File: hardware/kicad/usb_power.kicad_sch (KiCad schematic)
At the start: 9 parts, among them J801 USB-C, U801 USBLC6-2SC6, U802 LM66100DCKR

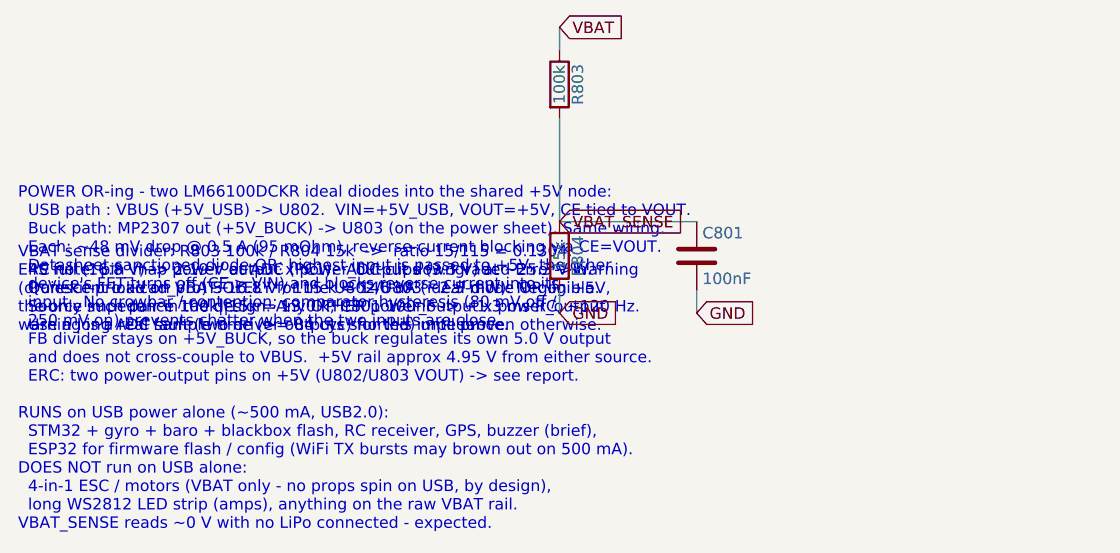
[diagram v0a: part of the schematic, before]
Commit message: Design review fixes: EN divider, +5V OR sizing, +5V bulk
- R106 43k -> 39k: MP2307 EN lockout 2.5V typ gives ~8.9 V turn-on and
  keeps EN < 6 V abs-max to 20 V input (was 6.0 V, zero margin)
- U803 LM66100 -> LM74700 + Q803 AO3400A: 1.5 A ceiling was below the
  ~1.9 A worst-case +5V budget; now FET-limited ~5 A at ~53 mV
- C113 22uF on the +5V OR node (was ~2 uF of LDO input caps only)
- ERC power_output x power_output reverted to Error; +5V now has a
  single power-output pin

Co-Authored-By: Claude Sonnet 5 <noreply@anthropic.com>
Claude-Session: https://claude.ai/code/session_0171uwNh8K8uwZuWio9f35u1
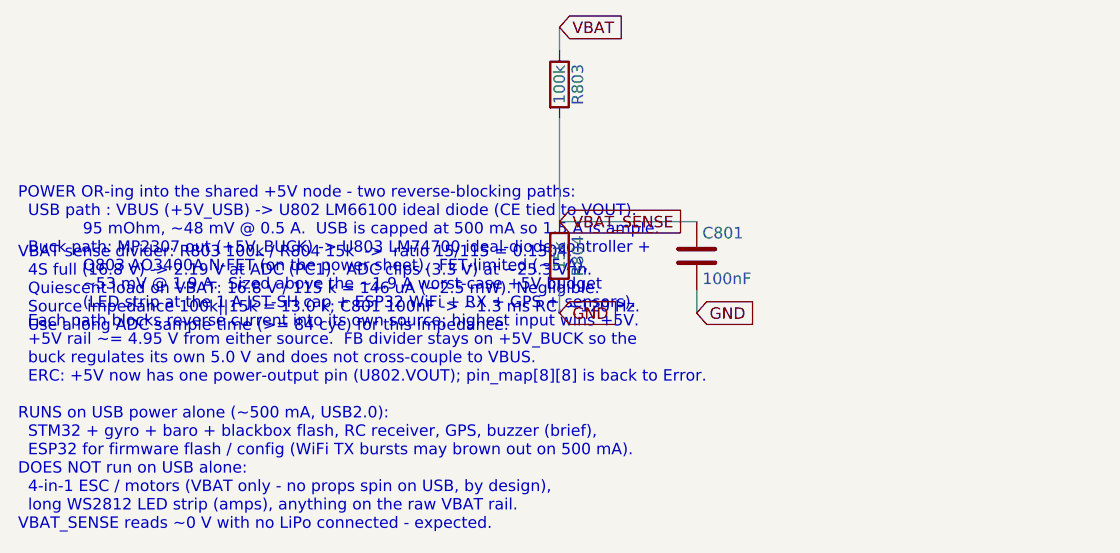
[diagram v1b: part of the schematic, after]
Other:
- note added: "POWER OR-ing into the shared +5V node - two reverse-blocking paths: USB path : VBUS (+5V_USB) -> U802 LM66100 ideal diode (CE tied to VOUT). 95 mOhm, ~48 mV @ 0.5 A. USB is capped at 500 mA so 1.5 A is ample. Buck path: MP2307 out (+5V_BUCK) -> U803 LM74700 ideal-diode controller + Q803 AO3400A N-FET (on the power sheet). FET-limited (~5 A), ~53 mV @ 1.9 A. Sized above the ~1.9 A worst-case +5V b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"
- note removed: "ERC note: pin_map power_output x power_output downgraded Error->Warning (dronekit-pro.kicad_pro) SOLELY for the U802/U803 ideal-diode OR on +5V, the only such pair in the design. Any OTHER power_output x power_output warning is a real fault (two driver outputs shorted) until proven otherwise."
- note removed: "POWER OR-ing - two LM66100DCKR ideal diodes into the shared +5V node: USB path : VBUS (+5V_USB) -> U802. VIN=+5V_USB, VOUT=+5V, CE tied to VOUT. Buck path: MP2307 out (+5V_BUCK) -> U803 (on the power sheet). Same wiring. Each: ~48 mV drop @ 0.5 A (95 mOhm), reverse-current blocking via CE=VOUT. Datasheet-sanctioned diode-OR: highest input is passed to +5V, the other device's FET turns off (CE > V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"
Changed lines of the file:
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@@
 		)
 	)
-  (text "POWER OR-ing - two LM66100DCKR ideal diodes into the shared +5V node:\n  USB path : VBUS (+5V_USB) -> U802.  VIN=+5V_USB, VOUT=+5V, CE tied to VOUT.\n  Buck path: MP2307 out (+5V_BUCK) -> U803 (on the power sheet). Same wiring.\n  Each: ~48 mV drop @ 0.5 A (95 mOhm), reverse-current blocking via CE=VOUT.\n  Datasheet-sanctioned diode-OR: highest input is passed to +5V, the other\n  device's FET turns off (CE > VIN) and blocks reverse current into its\n  input.  No crowbar / contention; comparator hysteresis (80 mV off /\n  250 mV on) prevents chatter when the two inputs are close.\n  FB divider stays on +5V_BUCK, so the buck regulates its own 5.0 V output\n  and does not cross-couple to VBUS.  +5V rail approx 4.95 V from either source.\n  ERC: two power-output pins on +5V (U802/U803 VOUT) -> see report.\n\nRUNS on USB power alone (~500 mA, USB2.0):\n  STM32 + gyro + baro + blackbox flash, RC receiver, GPS, buzzer (brief),\n  ESP32 for firmware flash / config (WiFi TX bursts may brown out on 500 mA).\nDOES NOT run on USB alone:\n  4-in-1 ESC / motors (VBAT only - no props spin on USB, by design),\n  long WS2812 LED strip (amps), anything on the raw VBAT rail.\nVBAT_SENSE reads ~0 V with no LiPo connected - expected."
+  (text "POWER OR-ing into the shared +5V node - two reverse-blocking paths:\n  USB path : VBUS (+5V_USB) -> U802 LM66100 ideal diode (CE tied to VOUT).\n             95 mOhm, ~48 mV @ 0.5 A.  USB is capped at 500 mA so 1.5 A is ample.\n  Buck path: MP2307 out (+5V_BUCK) -> U803 LM74700 ideal-diode controller +\n             Q803 AO3400A N-FET (on the power sheet).  FET-limited (~5 A),\n             ~53 mV @ 1.9 A.  Sized above the ~1.9 A worst-case +5V budget\n             (LED strip at the 1 A JST-SH cap + ESP32 WiFi + RX + GPS + sensors).\n  Each path blocks reverse current into its own source; highest input wins +5V.\n  +5V rail ~= 4.95 V from either source.  FB divider stays on +5V_BUCK so the\n  buck regulates its own 5.0 V and does not cross-couple to VBUS.\n  ERC: +5V now has one power-output pin (U802.VOUT); pin_map[8][8] is back to Error.\n\nRUNS on USB power alone (~500 mA, USB2.0):\n  STM32 + gyro + baro + blackbox flash, RC receiver, GPS, buzzer (brief),\n  ESP32 for firmware flash / config (WiFi TX bursts may brown out on 500 mA).\nDOES NOT run on USB alone:\n  4-in-1 ESC / motors (VBAT only - no props spin on USB, by design),\n  long WS2812 LED strip (amps), anything on the raw VBAT rail.\nVBAT_SENSE reads ~0 V with no LiPo connected - expected."
     (at 30 150 0)
     (effects (font (size 1.27 1.27)) (justify left bottom))
   )
-  (text "ERC note: pin_map power_output x power_output downgraded Error->Warning\n(dronekit-pro.kicad_pro) SOLELY for the U802/U803 ideal-diode OR on +5V,\nthe only such pair in the design. Any OTHER power_output x power_output\nwarning is a real fault (two driver outputs shorted) until proven otherwise."
-    (at 30 128 0)
-    (effects (font (size 1.27 1.27)) (justify left bottom))
-  )
